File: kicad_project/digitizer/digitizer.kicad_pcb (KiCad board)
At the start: 2 copper layers, 96 x 74 mm, 63 parts, among them IC201 MAX3059ASA+T UPSTREAM, IC202 MAX6035AAUR50+T, IC203 MAX3059ASA+T DOWNSTREAM, IC204 MAX6043BAUT33+T, IC301 ADS1234IPWR, J201 DT15-4P (UPSTREAM), J202 DT06-4S (DOWNSTREAM), J301 Load Cell 1, J302 Load Cell 2, J303 Load Cell 3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

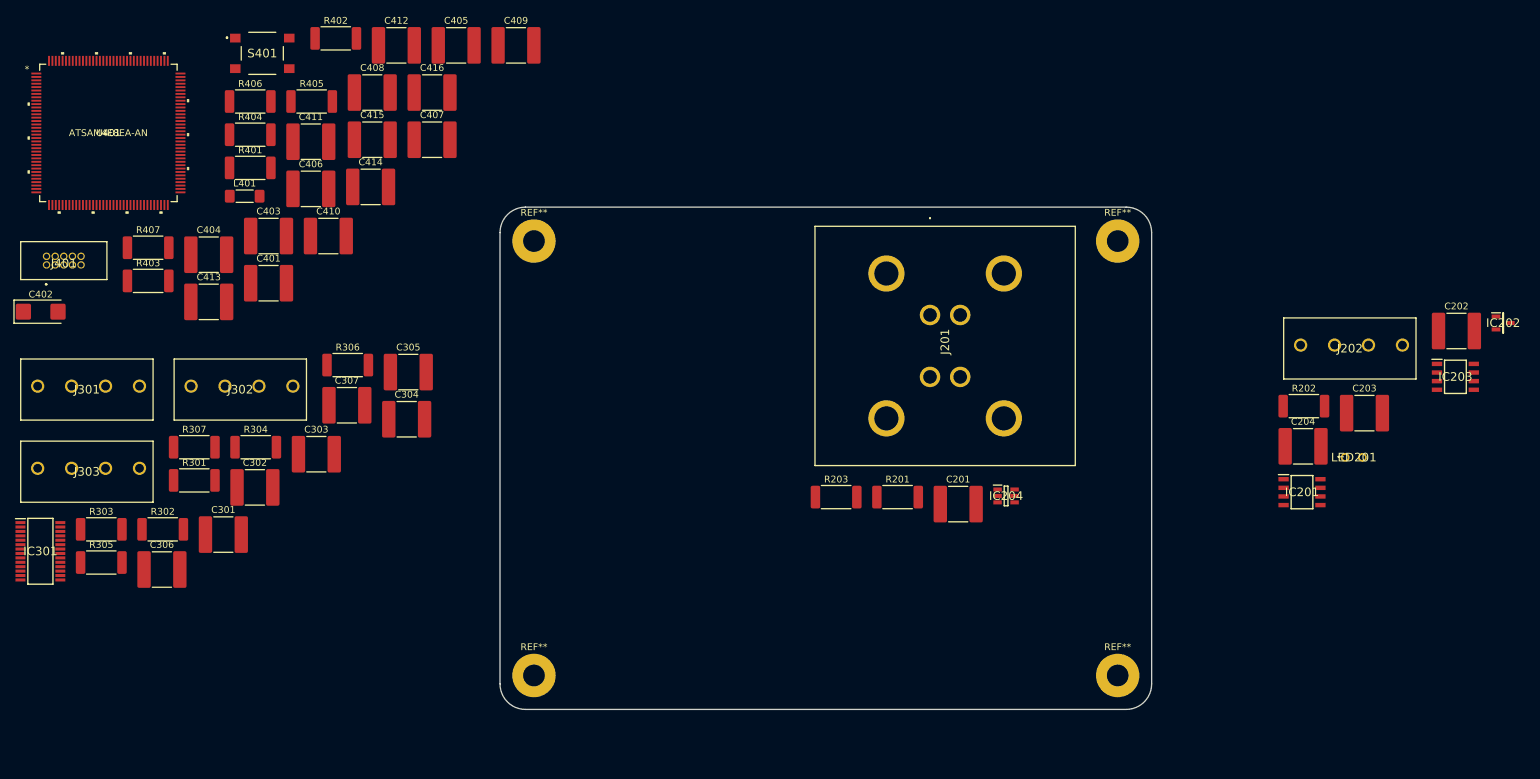
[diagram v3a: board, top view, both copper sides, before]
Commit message: placed all of the connectors and ICs in their initial spots/sides
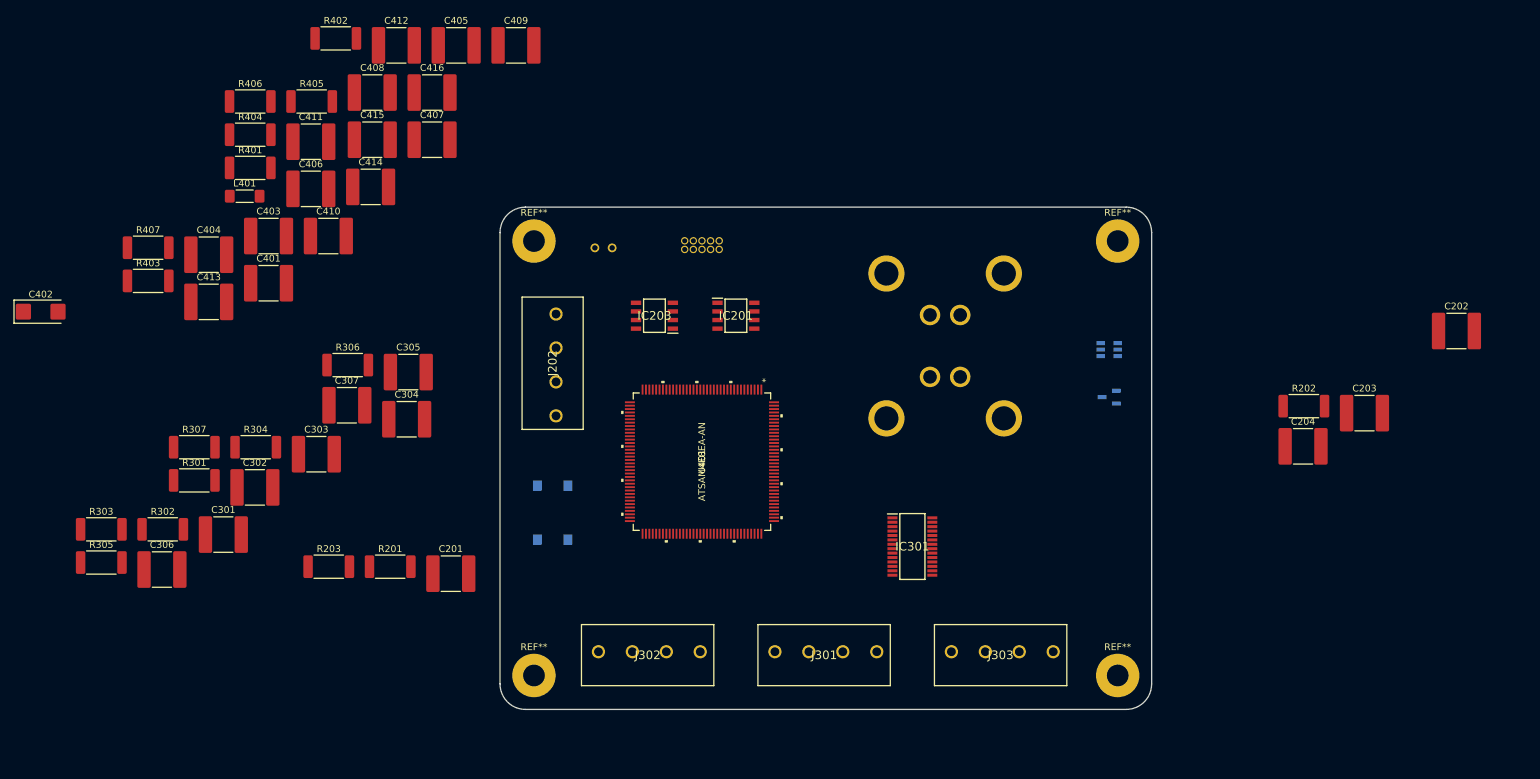
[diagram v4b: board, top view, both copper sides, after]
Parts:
- IC202, IC204, J201, J401, LED201, S401: moved to B.Cu
- moved J303 137.3 mm to (140.8, 114.5)
- moved IC301 128.5 mm to (135.0, 99.0)
- moved IC203 118.3 mm to (97.0, 65.0), turned to 180 degrees
- moved J301 115.4 mm to (114.8, 114.5)
- moved LED201 114.8 mm to (89.5, 55.0), turned to 180 degrees
- moved J202 109.8 mm to (82.5, 64.8), turned to -90 degrees
- moved U401 100.0 mm to (104.0, 86.5), turned to -90 degrees
- moved J401 99.1 mm to (106.5, 55.2), turned to 180 degrees
- moved IC201 87.4 mm to (109.0, 65.0)
- moved S401 80.0 mm to (82.0, 94.0), turned to -90 degrees
- moved C201 75.4 mm to (67.0, 103.0)
- moved R201 75.4 mm to (58.1, 102.0)
- moved R203 75.4 mm to (49.0, 102.0)
- moved J302 71.6 mm to (88.8, 114.5)
- moved IC202 59.1 mm to (164.0, 77.0), turned to 180 degrees
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
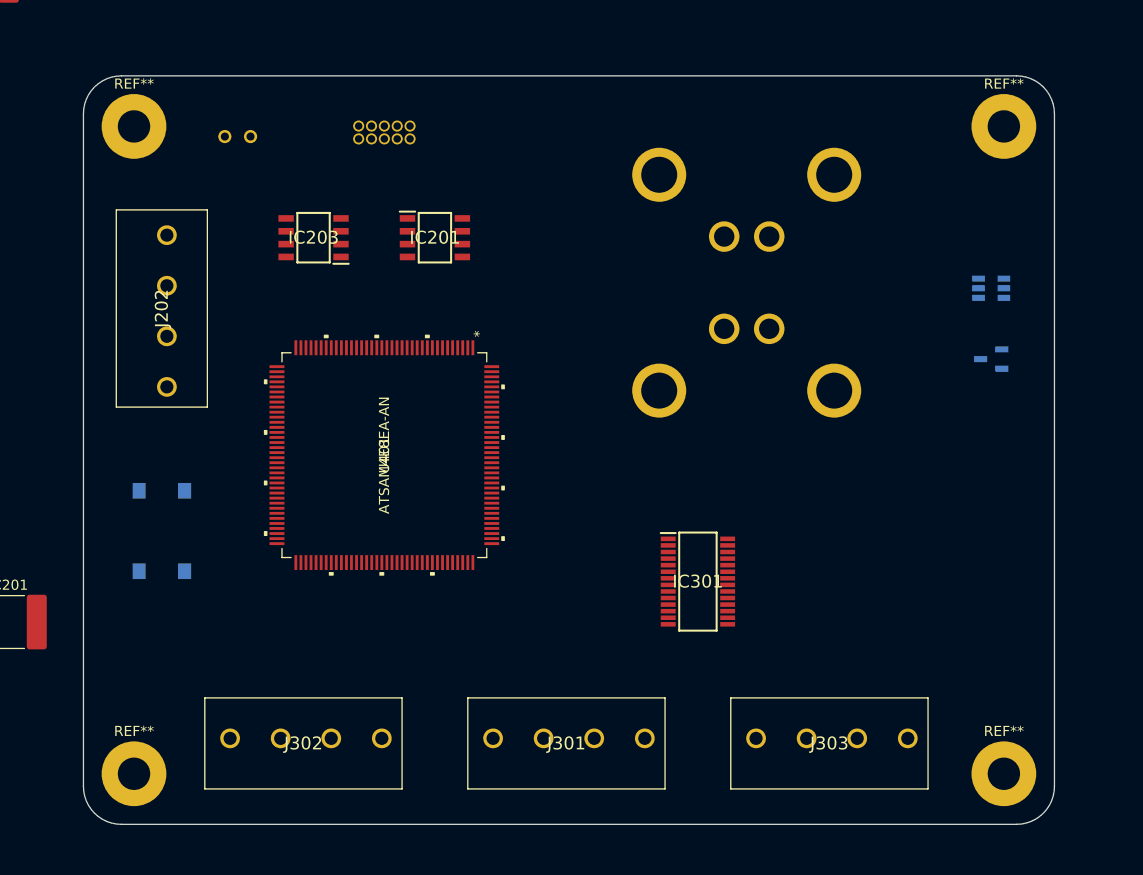
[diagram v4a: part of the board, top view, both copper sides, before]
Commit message: added a ground plane
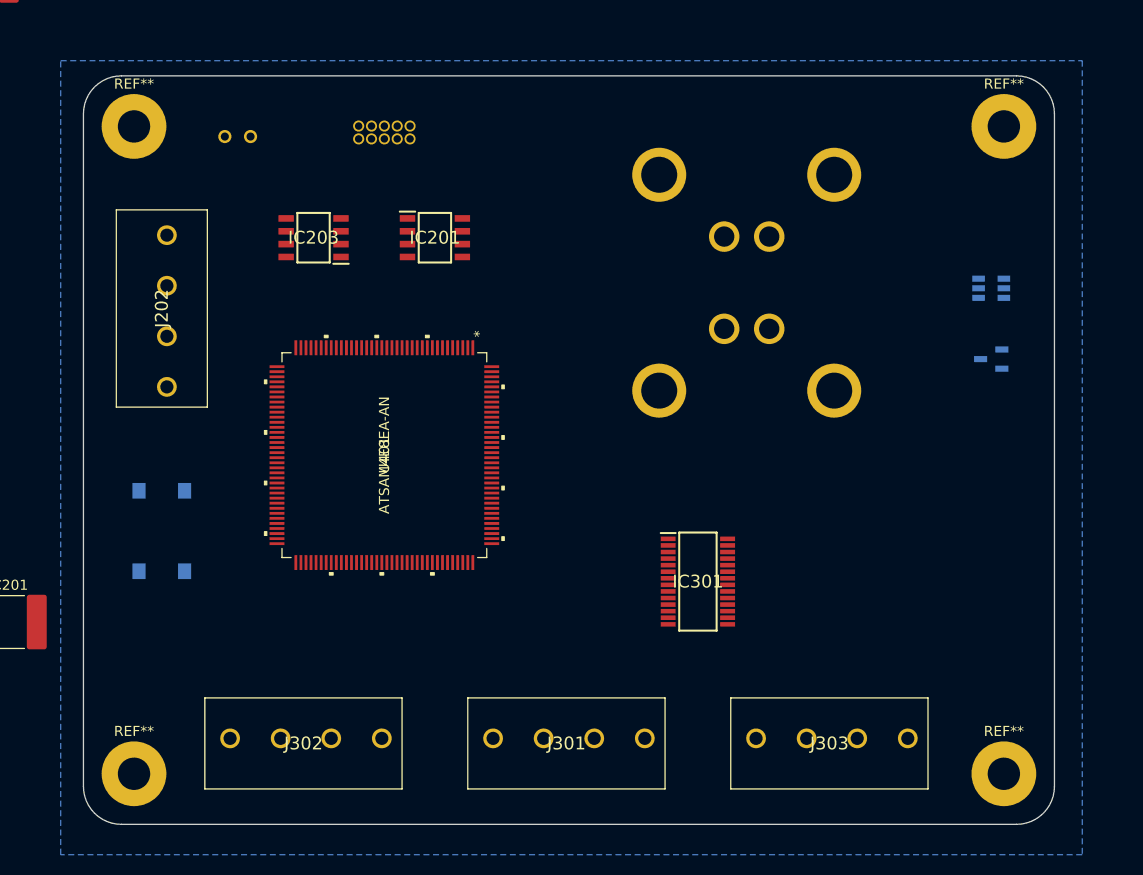
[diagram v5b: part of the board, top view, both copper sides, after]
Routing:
- added copper zone on B.Cu, net GND
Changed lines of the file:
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@@
       (effects (font (size 1 1) (thickness 0.15)))
     )
-    (fp_text user "0.011in/0.279mm" (at 8.75 -14.0462 90) (layer "Cmts.User")
+    (fp_text user "0.02in/0.5mm" (at 14.0462 -8.500001 90) (layer "Cmts.User")
+      (effects (font (size 1 1) (thickness 0.15)))
+    )
+    (fp_text user "0.836in/21.234mm" (at -15.5829 0 90) (layer "Cmts.User")
+      (effects (font (size 1 1) (thickness 0.15)))
+    )
+    (fp_text user "0.058in/1.473mm" (at 15.5829 -10.6172 90) (layer "Cmts.User")
       (effects (font (size 1 1) (thickness 0.15)))
     )
@@
       (effects (font (size 0.127 0.127) (thickness 0.002)))
     )
-    (fp_text user "0.058in/1.473mm" (at 15.5829 -10.6172 90) (layer "Cmts.User")
-      (effects (font (size 1 1) (thickness 0.15)))
-    )
     (fp_text user "0.836in/21.234mm" (at 0 15.3162 90) (layer "Cmts.User")
       (effects (font (size 1 1) (thickness 0.15)))
     )
-    (fp_text user "0.02in/0.5mm" (at 14.0462 -8.500001 90) (layer "Cmts.User")
-      (effects (font (size 1 1) (thickness 0.15)))
-    )
-    (fp_text user "0.836in/21.234mm" (at -15.5829 0 90) (layer "Cmts.User")
+    (fp_text user "0.011in/0.279mm" (at 8.75 -14.0462 90) (layer "Cmts.User")
       (effects (font (size 1 1) (thickness 0.15)))
     )
@@
     (fp_line (start -9.1437 -11.6078) (end 9.1437 -11.6078) (layer "F.CrtYd") (width 0.05))
     (fp_line (start -9.1437 11.6078) (end 9.1437 11.6078) (layer "F.CrtYd") (width 0.05))
+    (fp_line (start -10.2489 -9.1437) (end -10.2489 -10.2489) (layer "F.CrtYd") (width 0.05))
     (fp_line (start 10.2489 -9.1437) (end 10.2489 -10.2489) (layer "F.CrtYd") (width 0.05))
+    (fp_line (start 10.2489 9.1437) (end 11.6078 9.1437) (layer "F.CrtYd") (width 0.05))
     (fp_line (start 11.6078 -9.1437) (end 10.2489 -9.1437) (layer "F.CrtYd") (width 0.05))
     (fp_line (start 10.2489 -10.2489) (end 10.2489 -9.1437) (layer "F.CrtYd") (width 0.05))
@@
     (fp_line (start 11.6078 -9.1437) (end 11.6078 9.1437) (layer "F.CrtYd") (width 0.05))
     (fp_line (start 10.2489 10.2489) (end 9.1437 10.2489) (layer "F.CrtYd") (width 0.05))
-    (fp_line (start -11.6078 -9.1437) (end -10.2489 -9.1437) (layer "F.CrtYd") (width 0.05))
     (fp_line (start 9.1437 -10.2489) (end 10.2489 -10.2489) (layer "F.CrtYd") (width 0.05))
-    (fp_line (start 10.2489 9.1437) (end 11.6078 9.1437) (layer "F.CrtYd") (width 0.05))
     (fp_line (start 10.2489 9.1437) (end 10.2489 10.2489) (layer "F.CrtYd") (width 0.05))
     (fp_line (start -9.1437 11.6078) (end -9.1437 10.2489) (layer "F.CrtYd") (width 0.05))
     (fp_line (start -11.6078 9.1437) (end -11.6078 -9.1437) (layer "F.CrtYd") (width 0.05))
+    (fp_line (start -9.1437 -10.2489) (end -9.1437 -11.6078) (layer "F.CrtYd") (width 0.05))
     (fp_line (start -10.2489 10.2489) (end -9.1437 10.2489) (layer "F.CrtYd") (width 0.05))
+    (fp_line (start -11.6078 9.1437) (end -11.6078 -9.1437) (layer "F.CrtYd") (width 0.05))
     (fp_line (start 9.1437 -10.2489) (end 10.2489 -10.2489) (layer "F.CrtYd") (width 0.05))
-    (fp_line (start -10.2489 -9.1437) (end -10.2489 -10.2489) (layer "F.CrtYd") (width 0.05))
     (fp_line (start 9.1437 11.6078) (end 9.1437 10.2489) (layer "F.CrtYd") (width 0.05))
     (fp_line (start 9.1437 10.2489) (end 10.2489 10.2489) (layer "F.CrtYd") (width 0.05))
     (fp_line (start -10.2489 10.2489) (end -10.2489 9.1437) (layer "F.CrtYd") (width 0.05))
     (fp_line (start -10.2489 -10.2489) (end -9.1437 -10.2489) (layer "F.CrtYd") (width 0.05))
+    (fp_line (start -10.2489 9.1437) (end -11.6078 9.1437) (layer "F.CrtYd") (width 0.05))
     (fp_line (start 9.1437 -11.6078) (end 9.1437 -10.2489) (layer "F.CrtYd") (width 0.05))
     (fp_line (start -10.2489 9.1437) (end -11.6078 9.1437) (layer "F.CrtYd") (width 0.05))
-    (fp_line (start -10.2489 9.1437) (end -11.6078 9.1437) (layer "F.CrtYd") (width 0.05))
     (fp_line (start 10.2489 -9.1437) (end 11.6078 -9.1437) (layer "F.CrtYd") (width 0.05))
+    (fp_line (start 11.6078 9.1437) (end 11.6078 -9.1437) (layer "F.CrtYd") (width 0.05))
     (fp_line (start -9.1437 -11.6078) (end 9.1437 -11.6078) (layer "F.CrtYd") (width 0.05))
     (fp_line (start -9.1437 10.2489) (end -9.1437 11.6078) (layer "F.CrtYd") (width 0.05))
-    (fp_line (start -10.2489 10.2489) (end -10.2489 9.1437) (layer "F.CrtYd") (width 0.05))
-    (fp_line (start 11.6078 9.1437) (end 11.6078 -9.1437) (layer "F.CrtYd") (width 0.05))
-    (fp_line (start 10.2489 10.2489) (end 10.2489 9.1437) (layer "F.CrtYd") (width 0.05))
-    (fp_line (start -11.6078 9.1437) (end -11.6078 -9.1437) (layer "F.CrtYd") (width 0.05))
+    (fp_line (start 9.1437 -11.6078) (end 9.1437 -10.2489) (layer "F.CrtYd") (width 0.05))
+    (fp_line (start -11.6078 -9.1437) (end -10.2489 -9.1437) (layer "F.CrtYd") (width 0.05))
     (fp_line (start 9.1437 11.6078) (end -9.1437 11.6078) (layer "F.CrtYd") (width 0.05))
     (fp_line (start -11.6078 -9.1437) (end -10.2489 -9.1437) (layer "F.CrtYd") (width 0.05))
-    (fp_line (start -9.1437 -10.2489) (end -9.1437 -11.6078) (layer "F.CrtYd") (width 0.05))
+    (fp_line (start -10.2489 10.2489) (end -10.2489 9.1437) (layer "F.CrtYd") (width 0.05))
     (fp_line (start -10.2489 -9.1437) (end -10.2489 -10.2489) (layer "F.CrtYd") (width 0.05))
-    (fp_line (start 9.1437 -11.6078) (end 9.1437 -10.2489) (layer "F.CrtYd") (width 0.05))
+    (fp_line (start 10.2489 10.2489) (end 10.2489 9.1437) (layer "F.CrtYd") (width 0.05))
     (fp_line (start -5.1103 -10.9982) (end -5.3897 -10.9982) (layer "F.Fab") (width 0.1))
     (fp_line (start 7.6103 -10.9982) (end 7.6103 -9.9949) (layer "F.Fab") (width 0.1))
@@
   (gr_line (start 170.25 119.25) (end 170.25 52.75) (layer "Edge.Cuts") (width 0.1))
   (gr_arc (start 166.5 49) (mid 169.15165 50.09835) (end 170.25 52.75) (layer "Edge.Cuts") (width 0.1))
+  (zone (net 2) (net_name "GND") (layer "B.Cu") (name "GND_PLANE") (hatch edge 0.508)
+    (connect_pads (clearance 0.508))
+    (min_thickness 0.254) (filled_areas_thickness no)
+    (fill yes (thermal_gap 0.508) (thermal_bridge_width 0.508))
+    (polygon
+      (pts
+        (xy 173 126)
+        (xy 72 126)
+        (xy 72 47.5)
+        (xy 173 47.5)
+      )
+    )
+  )
 )

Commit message: added 5pin term blocks for the M12 connections, so we can properly ground the shield connections
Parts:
- IC202, IC204: moved to F.Cu
- J301, J302, J303: footprint SamacSys_Parts:1935187 -> SamacSys_Parts:1935190
- moved IC204 50.0 mm to (116.0, 56.0), turned to -90 degrees
- moved IC201 36.1 mm to (111.0, 101.0)
- moved IC203 36.1 mm to (99.0, 101.0)
- moved IC202 30.6 mm to (144.9, 101.0), turned to 0 degrees
- moved S401 28.4 mm to (104.0, 76.0), turned to 180 degrees
- moved J302 27.5 mm to (82.5, 87.7), turned to -90 degrees
- moved J301 18.8 mm to (96.0, 114.5)
- moved J303 10.8 mm to (130.0, 114.5)
- moved U401 10.5 mm to (103.0, 76.0)
- moved IC301 4.47 mm to (131.0, 101.0), turned to 90 degrees
- moved J202 1.00 mm to (82.5, 63.8)

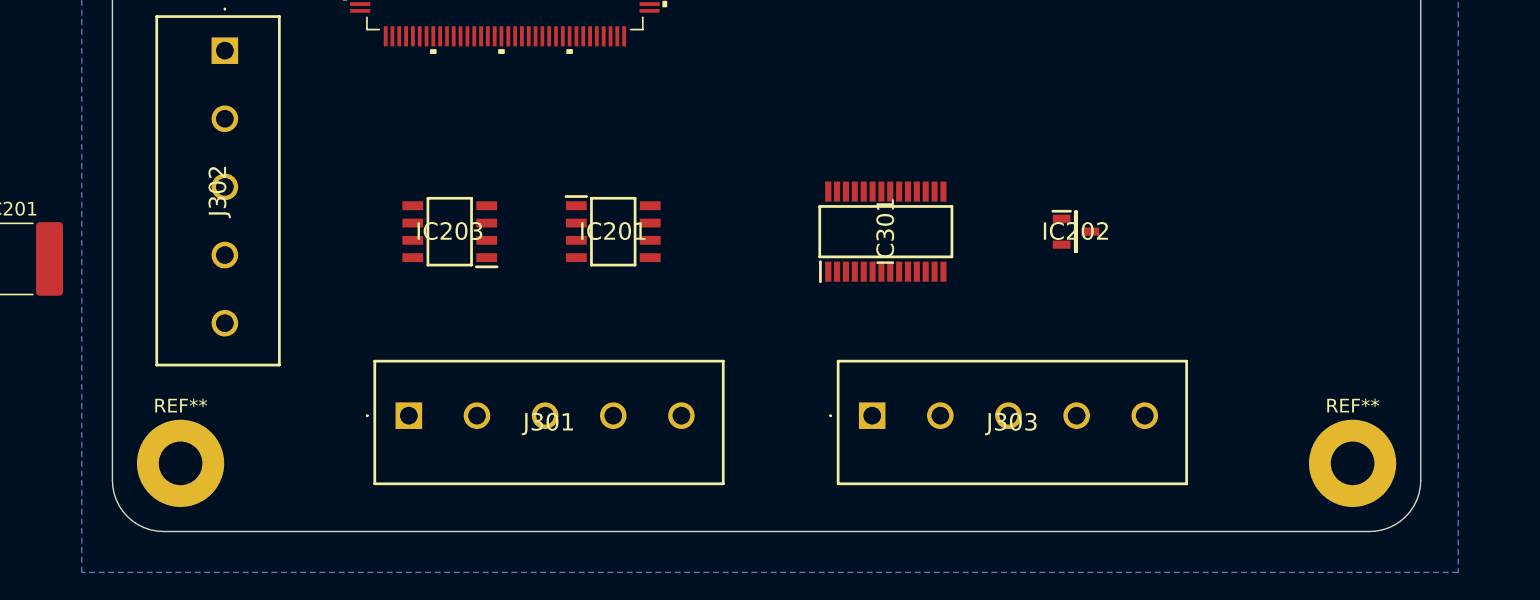
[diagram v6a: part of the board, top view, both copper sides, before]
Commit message: added plane for 5V clean on the F.Cu layer
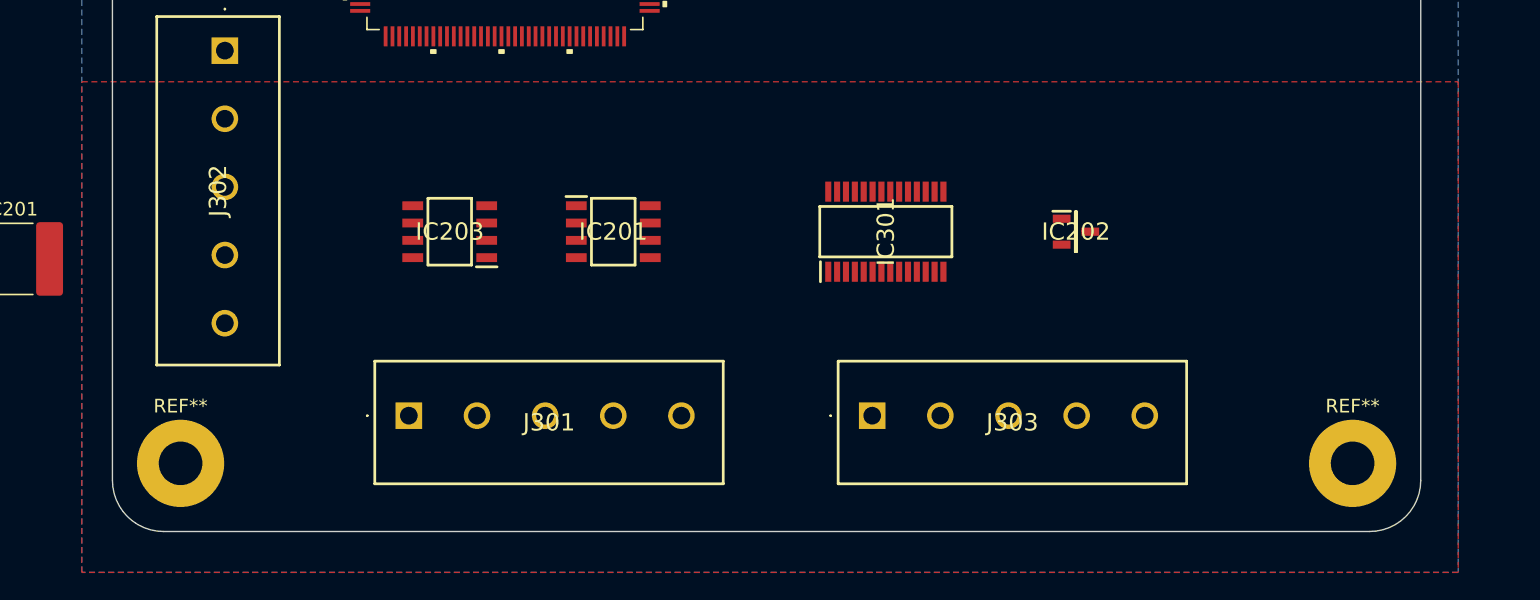
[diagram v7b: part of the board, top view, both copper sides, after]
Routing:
- added copper zone on F.Cu, net 5V_CLEAN
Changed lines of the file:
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@@
   (gr_line (start 170.25 119.25) (end 170.25 52.75) (layer "Edge.Cuts") (width 0.1))
   (gr_arc (start 166.5 49) (mid 169.15165 50.09835) (end 170.25 52.75) (layer "Edge.Cuts") (width 0.1))
+  (zone (net 3) (net_name "5V_CLEAN") (layer "F.Cu") (name "5V)CLEAN_PLANE") (hatch edge 0.508)
+    (connect_pads (clearance 0.508))
+    (min_thickness 0.254) (filled_areas_thickness no)
+    (fill yes (thermal_gap 0.508) (thermal_bridge_width 0.508))
+    (polygon
+      (pts
+        (xy 173 126)
+        (xy 72 126)
+        (xy 72 90)
+        (xy 173 90)
+      )
+    )
+  )
   (zone (net 2) (net_name "GND") (layer "B.Cu") (name "GND_PLANE") (hatch edge 0.508)
     (connect_pads (clearance 0.508))
